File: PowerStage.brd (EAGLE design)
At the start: 100 x 100 mm, 97 parts, among them IC1 FSBB30CH60, IC2 HCNR200, IC4 LM358D, IC5 HCNR200, IC6 78L05F, Q1 BC817-16SMD, X1 MKDSN1,5/2-5,08, X2 MKDSN1,5/3-5,08

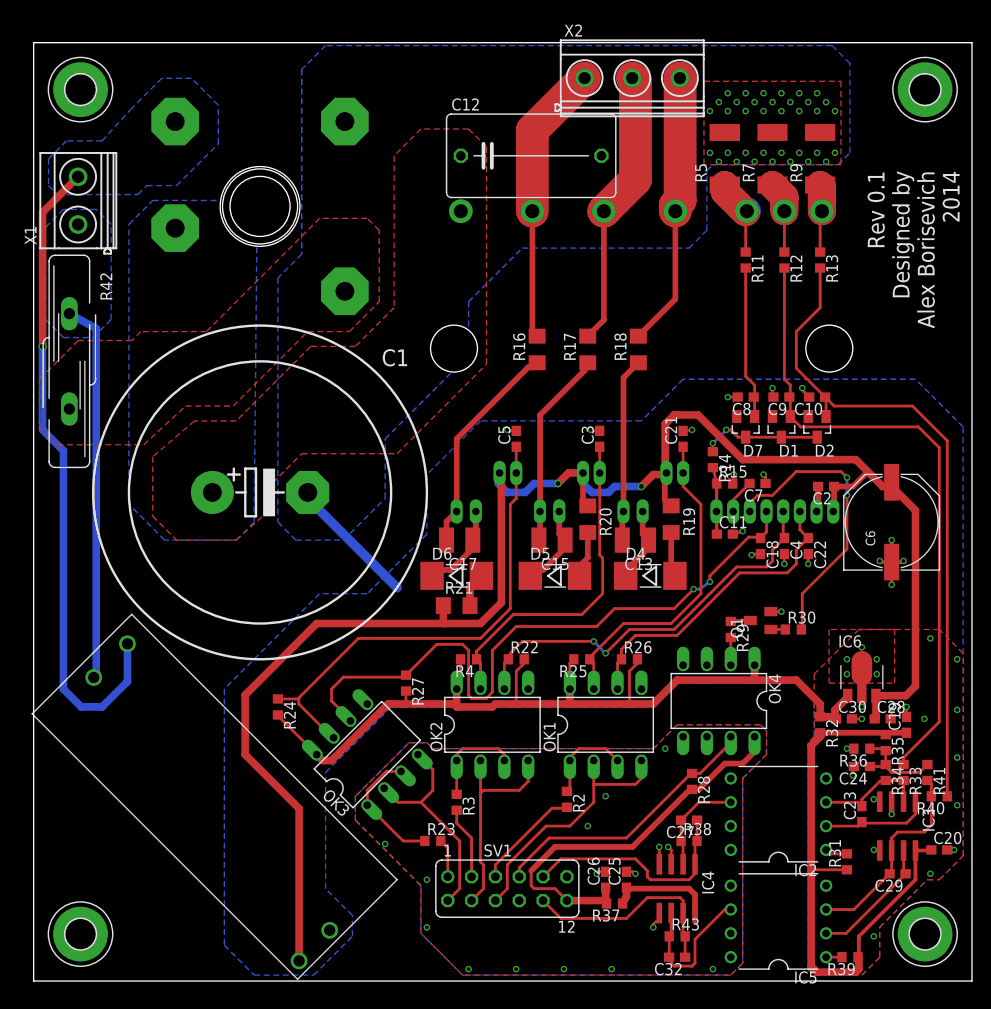
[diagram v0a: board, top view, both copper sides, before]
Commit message: Stable version
Tested at  1 kW motor
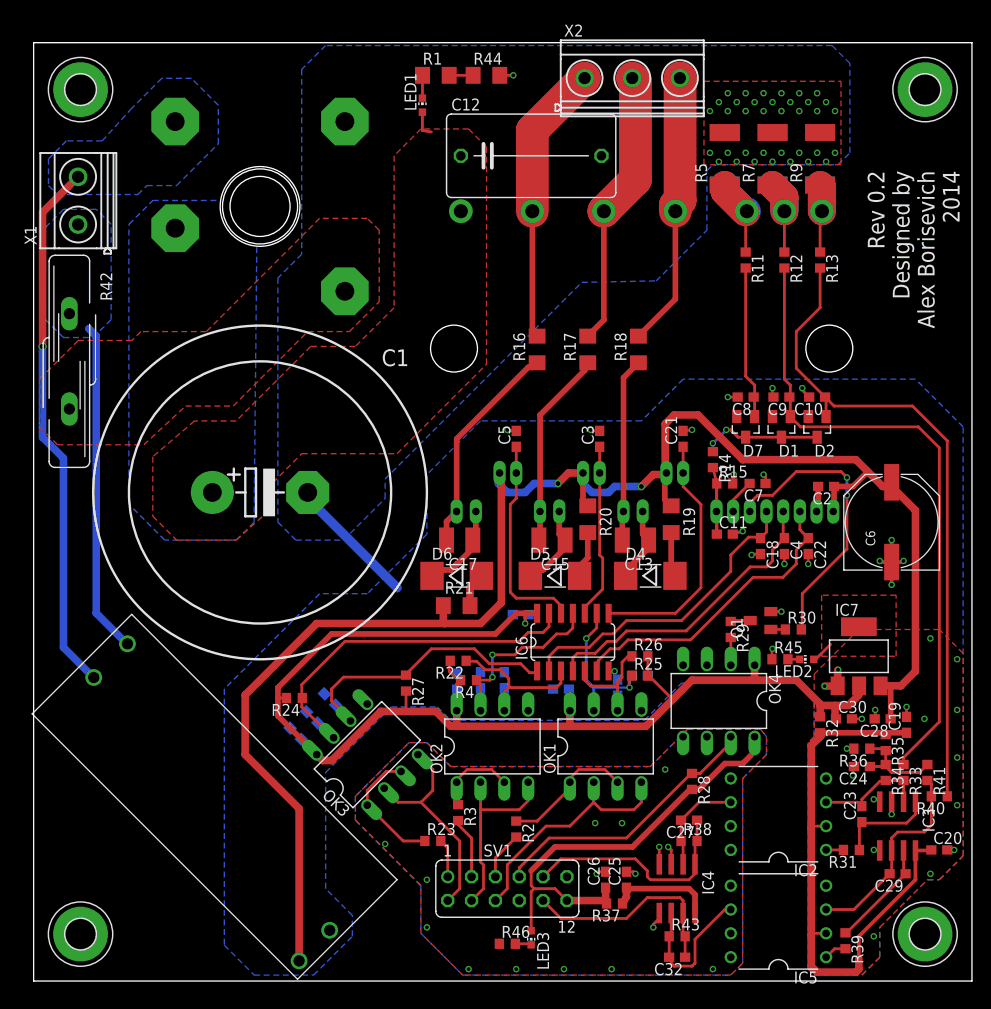
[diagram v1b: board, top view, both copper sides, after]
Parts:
- added C14, C16, C31, C33: 0.1 uF, rcl:C0603
- added C34, C35, C36, C37, C38, C39: 10 nF, rcl:C0603
- added IC7: REG1117, burr-brown:SOT223
- added LED1, LED2, LED3: (no value), led:CHIP-LED0603
- added R1, R44: 68 k, resistor:R1206
- added R45, R46: 220, rcl:R0603
- IC6: value 78L05F -> 74HCT04D; device linear:SOT89 -> 74xx-eu:SO14
- R33, R34, R40, R41: value 15 k -> 33 k
- moved IC6 31.0 mm to (57.5, 36.1)
- moved R25 6.43 mm to (64.6, 32.5), turned to 0 degrees
- moved R2 6.26 mm to (51.4, 16.2)
- moved R22 6.19 mm to (45.2, 34.1), turned to 180 degrees
- moved OK1 2.30 mm to (61.0, 25.0)
- moved OK2 2.30 mm to (48.9, 25.0)
- moved R4 2.22 mm to (46.4, 32.1)
- moved R24 1.99 mm to (27.8, 30.2), turned to 180 degrees
- moved R39 1.81 mm to (86.5, 4.29), turned to 270 degrees
- moved R31 1.36 mm to (87.2, 14.0), turned to 180 degrees
- moved R26 1.16 mm to (64.6, 34.6)
- moved R3 1.12 mm to (45.2, 17.9)
- turned C28 to 180 degrees
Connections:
- removed net N$4: B1.AC2-, U$1.AC2, X1.2
- new net N$33: C39.1, IC6.9, OK1.7, R25.1
- new net N$39: C38.1, IC6.5, OK1.6, R26.1
- new net N$40: C37.1, IC6.11, OK2.7, R4.1
- new net N$41: C36.1, IC6.3, OK2.6, R22.1
- new net N$42: C35.1, IC6.13, OK3.7, R24.1
- new net N$43: C34.1, IC6.1, OK3.6, R27.1
- new net N$44: LED1.C, R1.1
- new net N$45: R1.2, R44.1
- new net N$46: LED2.C, R45.2
- new net N$47: LED3.C, R46.2
- new net N$48: R42.1, U$1.AC2, X1.1
- net +15V: now also IC7.3; no longer IC6.3
- net +300V: now also LED1.A
- net +5V: now also C14.1, C16.1, C31.1, C33.1, IC6.14, IC7.2, IC7.4, LED2.A; no longer IC6.1
- net GND: now also C14.2, C16.2, C31.2, C33.2, C34.2, C35.2, C36.2, C37.2, C38.2, C39.2, IC6.7, IC7.1, R44.2, R45.1; no longer IC6.2, IC6.2@1
- net GNDIO: now also R46.1
- net INUH: now also IC6.8; no longer OK1.7, R25.1
- net INUL: now also IC6.6; no longer OK1.6, R26.1
- net INVH: now also IC6.10; no longer OK2.7, R4.1
- net INVL: now also IC6.4; no longer OK2.6, R22.1
- net INWH: now also IC6.12; no longer OK3.7, R24.1
- net INWL: now also IC6.2; no longer OK3.6, R27.1
- net N$35: now also R39.1; no longer IC5.2
- net N$36: now also R31.1; no longer IC2.2
- net N$5: now also B1.AC2-, X1.2; no longer R42.1, X1.1
- net VCCA: now also IC2.2, IC5.2; no longer R31.1, R39.1
- net VCCIO: now also LED3.A
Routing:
- net N$4: track 70.0 -> 0.00 mm, vias 1 -> 0
- net +5V: track 94.3 -> 132.8 mm, vias 0 -> 1
- net N$42: track 0.00 -> 37.5 mm
- net INWL: track 70.9 -> 33.9 mm, vias 2 -> 0
- net N$48: track 0.00 -> 35.4 mm
- net INWH: track 52.1 -> 22.6 mm
- net N$43: track 0.00 -> 29.3 mm
- net N$40: track 0.00 -> 19.0 mm, vias 0 -> 2
- net N$33: track 0.00 -> 17.9 mm, vias 0 -> 2
- net INVH: track 36.0 -> 18.7 mm
- net N$5: track 40.6 -> 57.3 mm, vias 0 -> 1
- net N$41: track 0.00 -> 16.1 mm
- net N$39: track 0.00 -> 11.4 mm
- net INVL: track 43.0 -> 32.8 mm, vias 2 -> 0
- net INUH: track 35.0 -> 26.8 mm
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- added copper zone on layer 1, net +5V
- added copper zone on layer 16, net N$48
- removed copper zone on layer 16, net N$4
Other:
- board text added: "Rev 0.2 Designed by Alex Borisevich 2014"
- board text removed: "Rev 0.1 Designed by Alex Borisevich 2014"
